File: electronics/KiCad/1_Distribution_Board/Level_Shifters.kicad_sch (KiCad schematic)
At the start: 32 parts, among them J10 Generic 2.54mm, J11 Generic 2.54mm, J5 Generic 2.54mm, J6 Generic 2.54mm, J8 Generic 2.54mm, J9 Generic 2.54mm, Q2 AO3400A, Q3 AO3400A, Q4 AO3400A, Q5 AO3400A

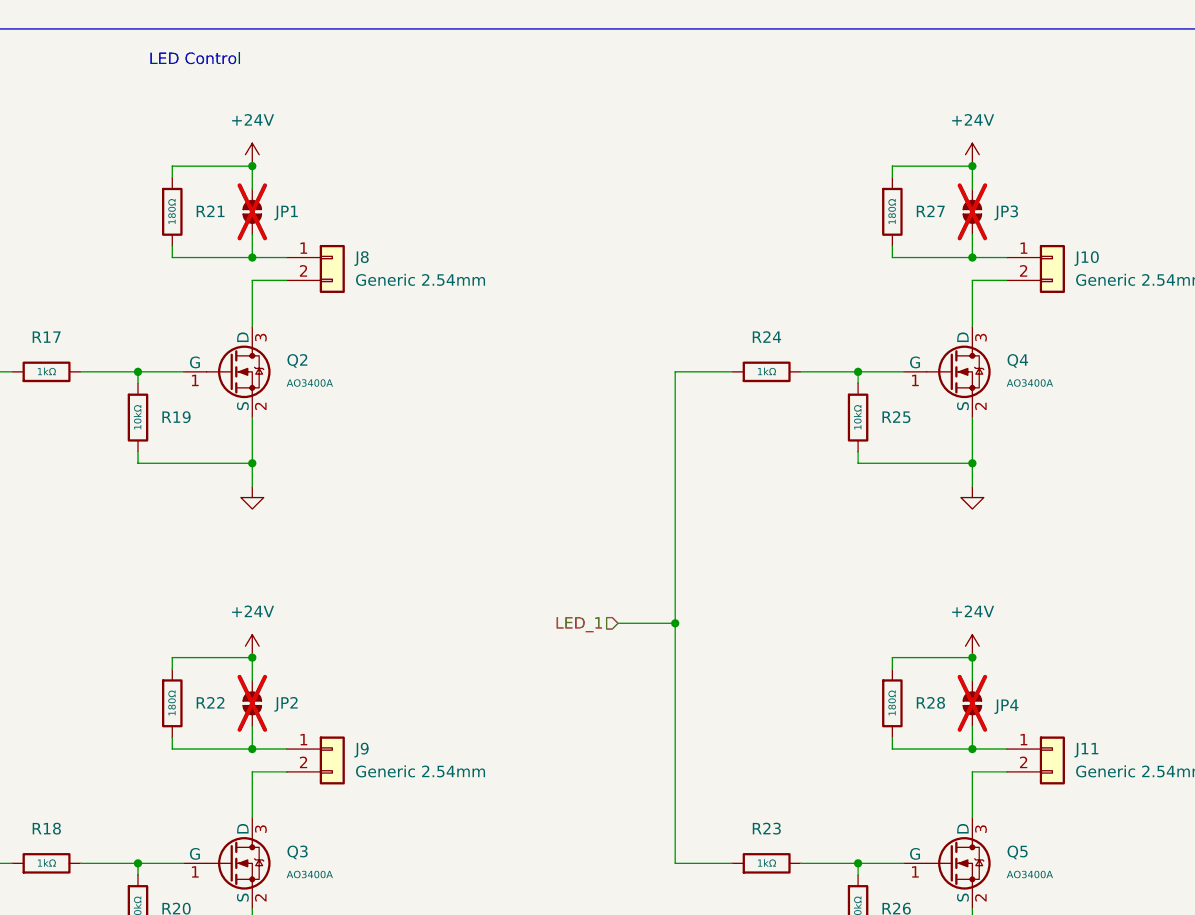
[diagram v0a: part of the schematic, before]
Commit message: distribution board v1.4: hardwired driver addresses, led ports on 24 v, no module headers, fill-only logo, rev in silkscreen
Stepper driver UART addresses are now fixed in copper:
- Removed the ten MS1/MS2 jumper headers (J21, J22, J25, J26, J29, J30,
  J33, J34, J37, J38) and the twenty 10k resistors that served only them
  (R61-R64, R67-R70, R73-R76, R79-R82, R85-R88). The DIAG pull-ups R13,
  R16, R65, R66 and R71 stay, and so does R72, the series resistor of
  the VSYS LED D7.
- Each driver's MS1 (AD0) and MS2 (AD1) pins are tied straight to GND or
  +3V3 through new sheet pins on the root sheet: A2 = 0, A3 = 1, A4 = 2,
  A5 = 3 on UART0 and A6 = 0 on UART1. This is the address map the
  firmware already uses (TMC_UART_ADDRESSES), so firmware does not change.
- On the board the low pins join the ground pour, two of them through a
  short ground stitch and via, and the high pins get short bottom-layer
  +3V3 tracks. Tracks and vias that only served the jumpers are removed.
- Removed the jumper silkscreen: the Pins/Setting legend, the "1 2 3" and
  "3 2 1" pin numbers, the MS1/MS2 labels and "!Double check!".
- The Stepper_Module sheet loses its jumper block and microstep table; a
  note on the root sheet gives the address map.

LED and fan ports run straight from 24 V:
- Removed the 180 ohm resistors R21, R22, R27, R28 and the bypass solder
  jumpers JP1-JP4. Pin 1 of J8, J9, J10 and J11 now connects directly to
  +24V, the state v1.3 boards were built in with the bypasses bridged.
- Removed the four "Bypass Rxx" labels.

Plug-in PCA9685 module headers removed:
- Removed J14, J15, J16, J18, J19 and J20, the module's silkscreen outline,
  the "A10" label and the three tracks that only went to J16. A new ground
  via replaces J16's ground pin as the stitch for that patch of ground pour.
- The on-board PCA9685 (U7) and everything it uses stay, including the
  220 ohm output resistors R43-R58 on the path to J17 and J12.

Oscillator follow-ups:
- D1 (MBR120VLSFT1G, LC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
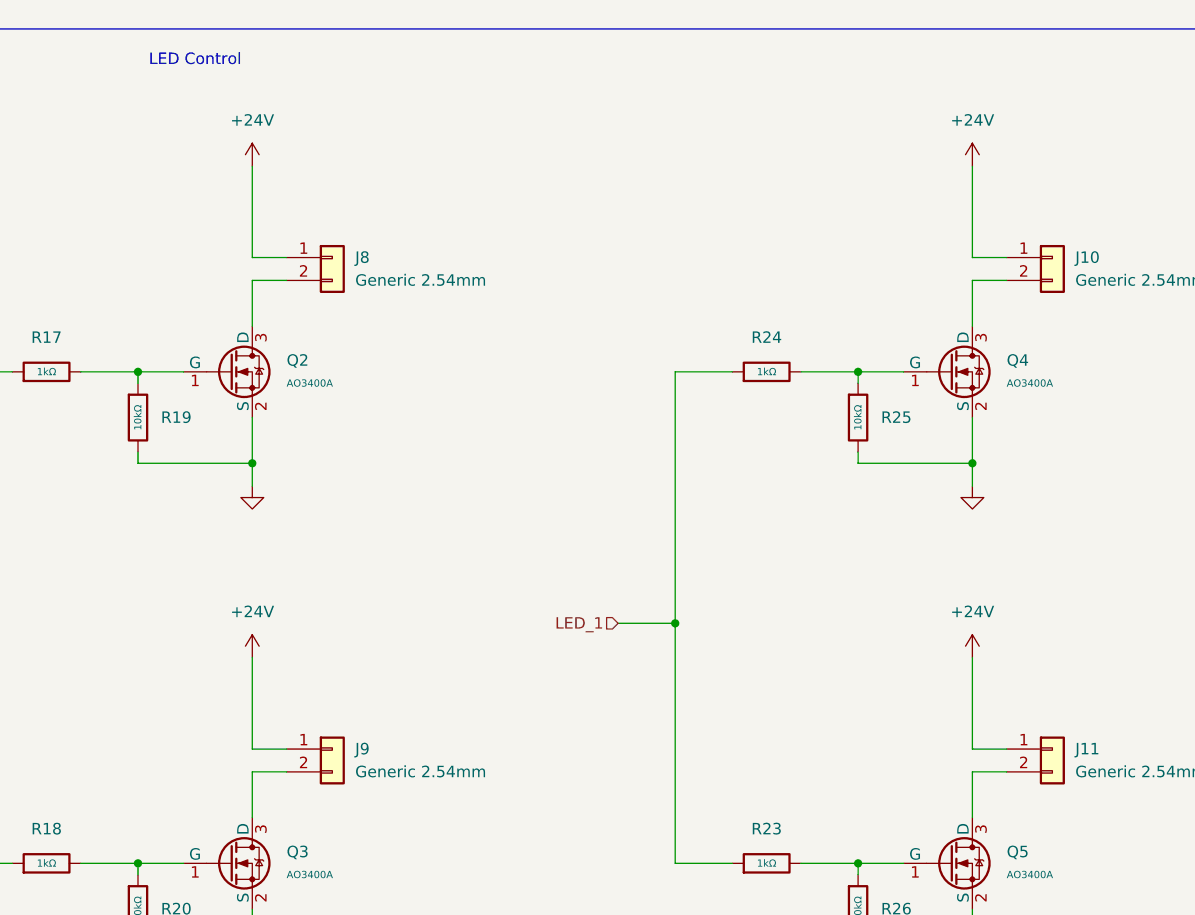
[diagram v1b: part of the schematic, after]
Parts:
- removed JP1, JP2, JP3, JP4: (no value), PCM_SparkFun-Jumper:Jumper_2_NO, symbol PCM_SparkFun-Jumper:SolderJumper_2_Open
- removed R21, R22, R27, R28: 180Ω, PCM_JLCPCB:R_1206, symbol PCM_JLCPCB-Resistors:1206,180Ω
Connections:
- net +24V: now also J10.1 (Pin_1), J11.1 (Pin_1), J8.1 (Pin_1), J9.1 (Pin_1)
